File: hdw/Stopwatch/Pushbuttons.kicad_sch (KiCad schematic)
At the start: 41 parts, among them SW701 Cap_Touch, SW702 Cap_Touch, SW703 Cap_Touch, U701 AT42QT1010-TSHR, U702 TLV71330PDBV, U703 TLV71330PDBV, U704 74LVC1G80, U705 74LVC1G17, U706 TLV71330PDBV, U707 AT42QT1010-TSHR, U708 AT42QT1010-TSHR, U709 74LVC1G17, U710 74LVC1G17

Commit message: started sch work
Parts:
- removed C704, C707, C708, C709, C715: 0.1uF, Capacitors_SMD:C_0603, symbol Custom_Library:C_Custom
- removed C706: 10nF, Capacitors_SMD:C_0603, symbol Custom_Library:C_Custom
- removed C711: 10uF, Capacitors_SMD:C_0603, symbol Custom_Library:C_Custom
- removed R703: 499, Resistors_SMD:R_0603, symbol Custom_Library:R_Custom
- removed R710, R?: 10k, Resistors_SMD:R_0603, symbol Custom_Library:R_Custom
- removed SW703: Cap_Touch, Custom Footprints Library:Capacitive_Touch_Pad, symbol Custom_Library:Cap_Touch
- removed U702, U703, U706: TLV71330PDBV, Package_TO_SOT_SMD:SOT-23-5, symbol Incrementor-rescue:TLV71330PDBV-Regulator_Linear
- removed U705, U709, U710: 74LVC1G17, TO_SOT_Packages_SMD:SOT-353_SC-70-5, symbol Custom_Library:74LVC1G17_Power
- removed U708: AT42QT1010-TSHR, TO_SOT_Packages_SMD:SOT-23-6, symbol Sensor_Touch:AT42QT1010-TSHR
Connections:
- net +3V3: now also U701.5 (VDD), U701.6 (SYNC), U707.5 (VDD), U707.6 (SYNC)
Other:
- moved on the sheet: C701, C702, C703, C705, C712, C713, C717, R701, R702, R708, R709, R712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

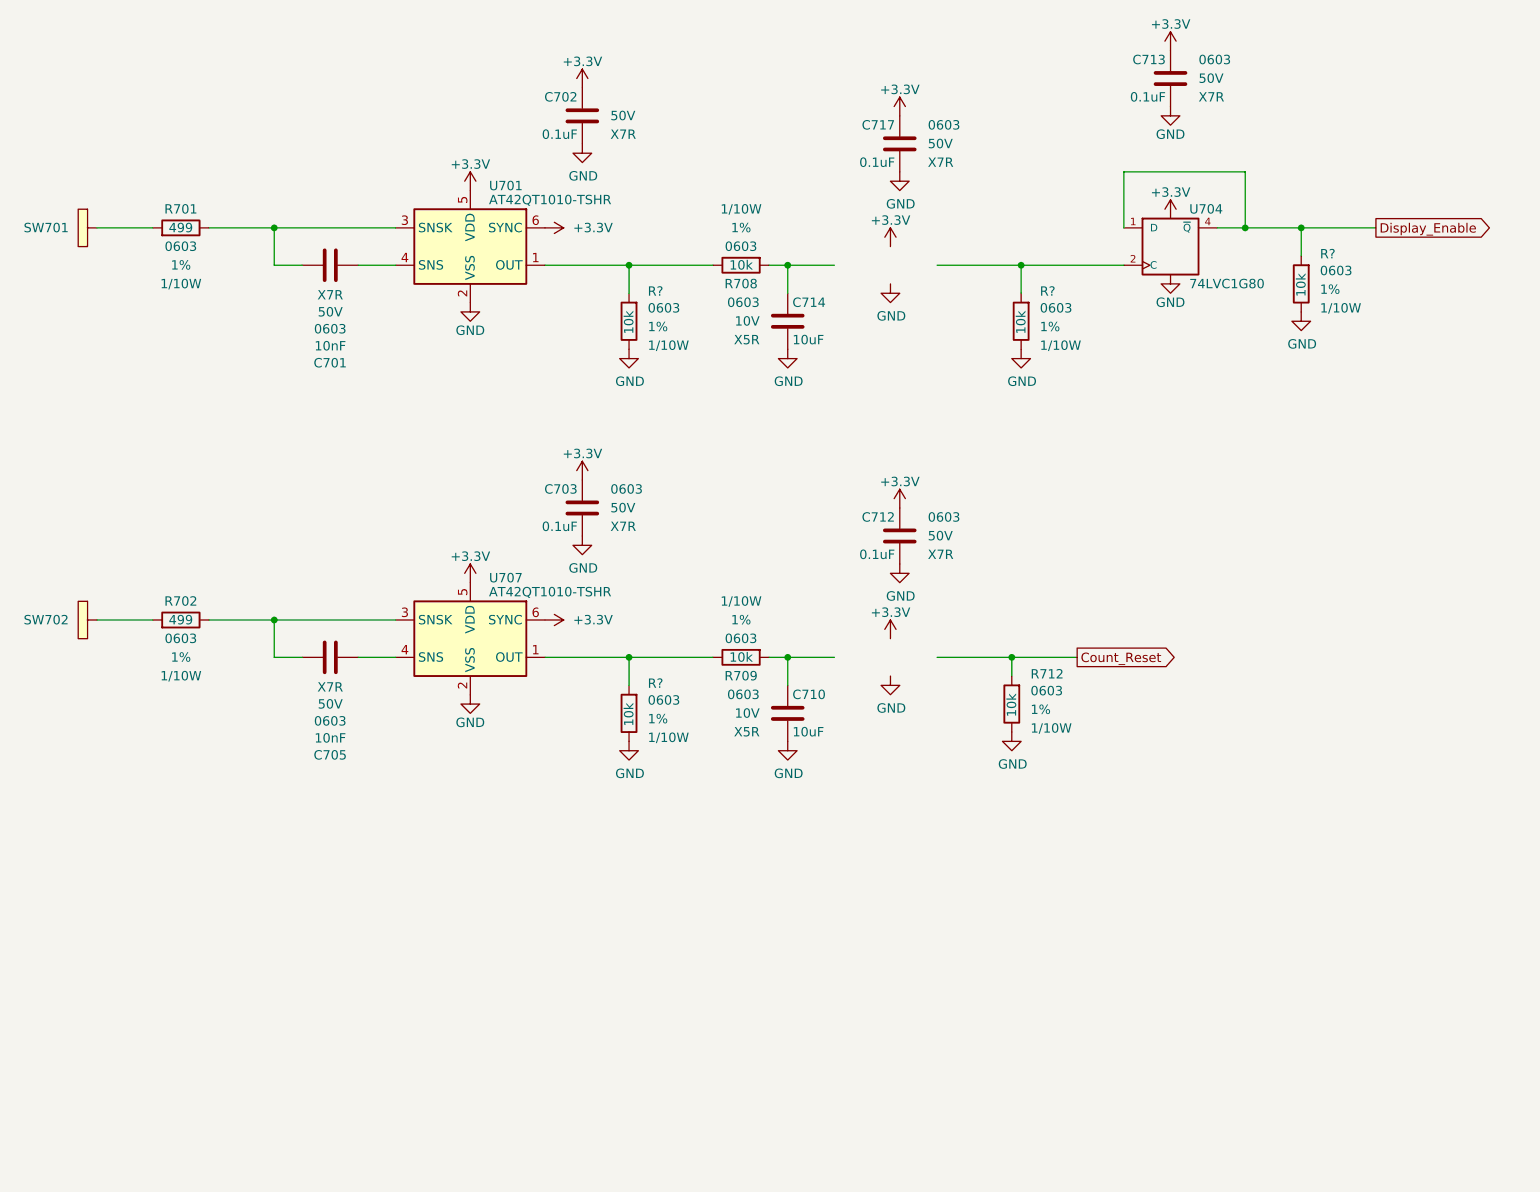
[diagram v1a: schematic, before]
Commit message: adjusted stage sheet
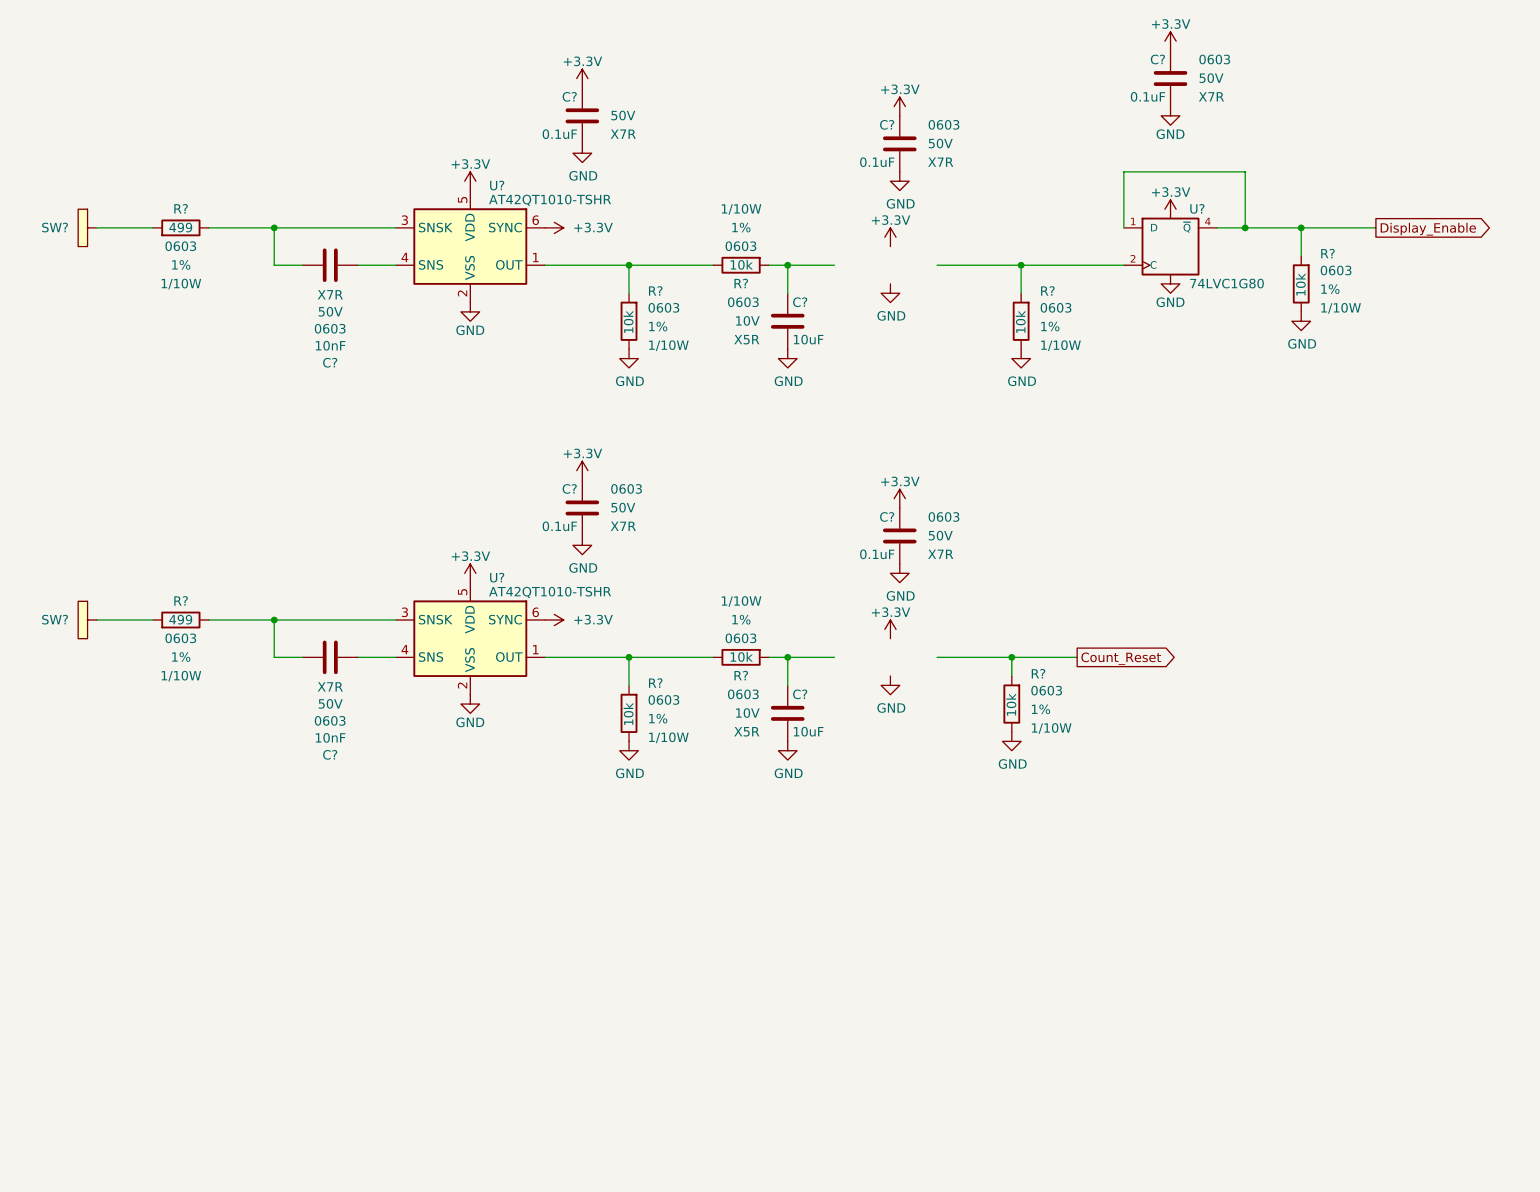
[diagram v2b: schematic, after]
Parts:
- renumbered C701 to C?, C713 to C?, C714 to C?, C702 to C?, C717 to C?, C705 to C?, C710 to C?, C712 to C?, C703 to C?, R701 to R?, R708 to R?, R712 to R?, R702 to R?, R709 to R?, SW701 to SW?, SW702 to SW?, U701 to U?, U704 to U?, U707 to U?

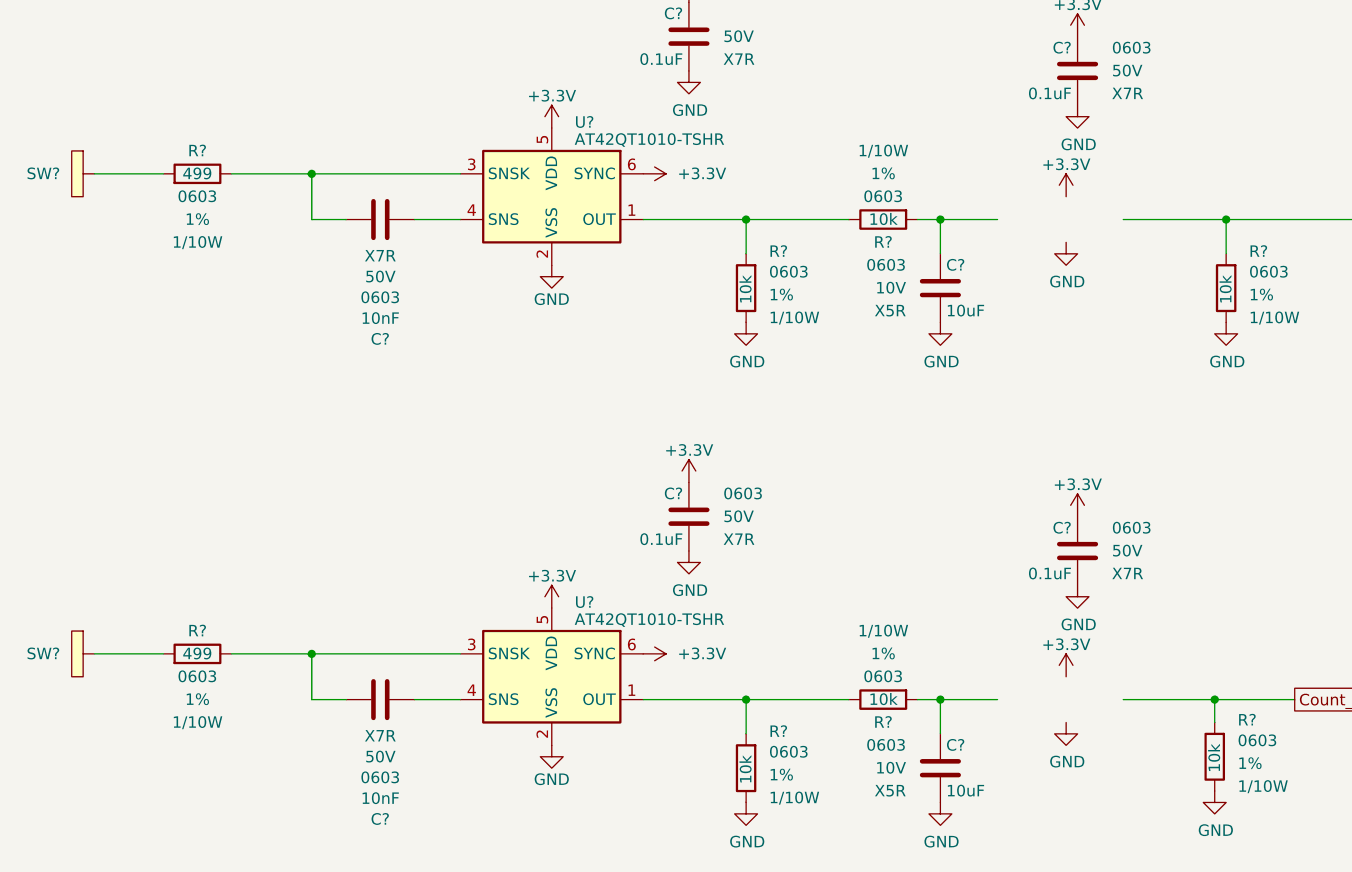
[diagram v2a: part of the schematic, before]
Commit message: added reset stuff
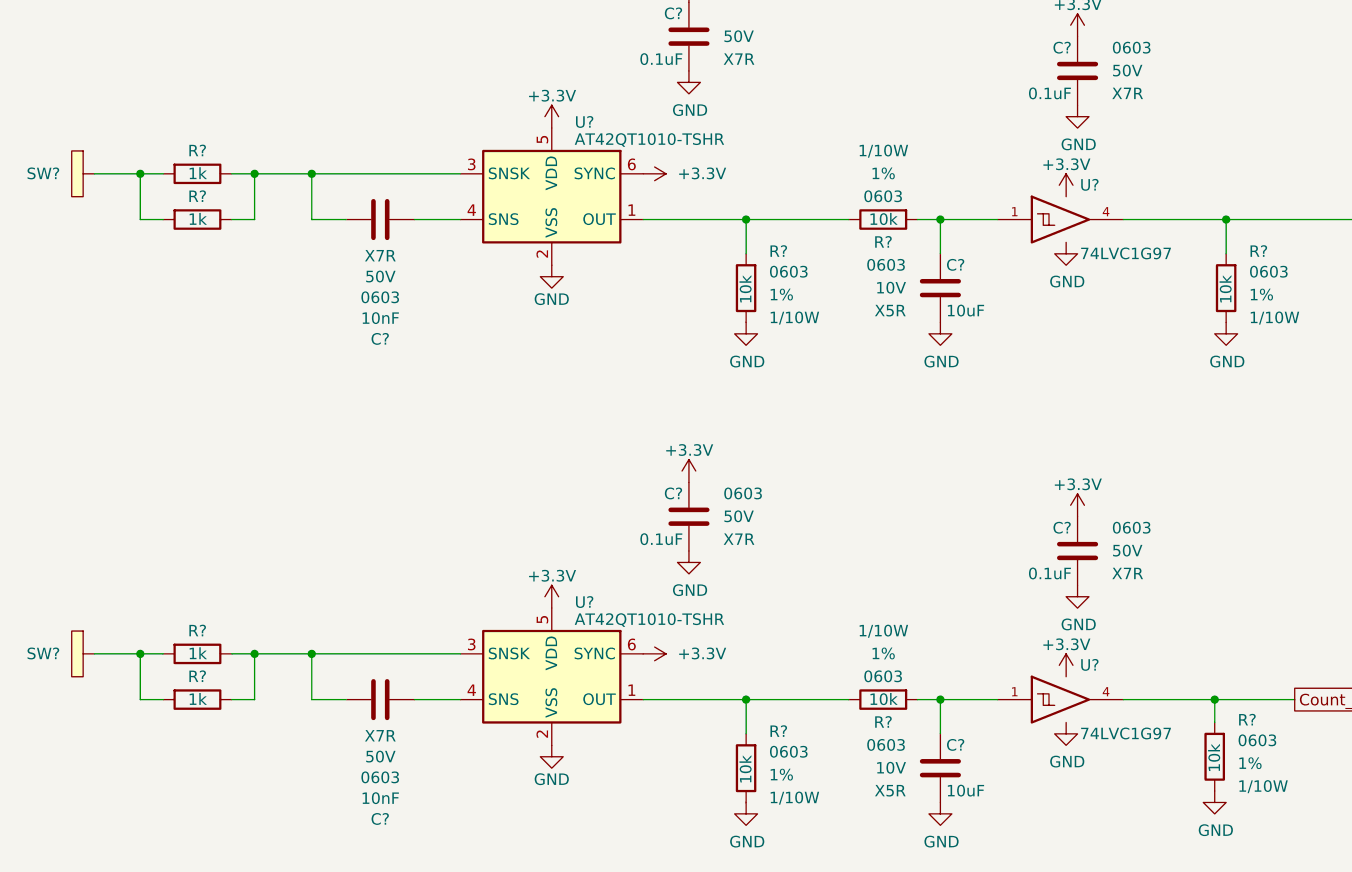
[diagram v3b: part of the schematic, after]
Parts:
- removed R? (x2): 499, Resistors_SMD:R_0603, symbol Custom_Library:R_Custom
- added R? (x4): 1k, Resistors_SMD:R_0603, symbol Custom_Library:R_Custom
- added U? (x2): 74LVC1G97, Package_TO_SOT_SMD:SOT-363_SC-70-6, symbol Custom Library:74LVC1G97_Power_BUF
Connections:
- net +3V3: now also U?.5 (VCC), U?.5 (VCC)
- net Count_Reset: now also U?.4
- net GND: now also U?.2 (GND), U?.2 (GND), U?.3 (GND), U?.3 (GND), U?.6 (GND), U?.6 (GND)
- net at C?.2, U?.3 (SNSK): now also R?.2, R?.2 (x2)
- net at SW?.1 (TP): now also R?.1, R?.1 (x2)
- net at R?.1, U?.2 (C): now also U?.4
- net at C?.1, R?.1: now also U?.1 (x2)

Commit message: added some more junk
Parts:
- added C?: 10nF, Capacitors_SMD:C_0603, symbol Custom_Library:C_Custom
- added C? (x3): 0.1uF, Capacitors_SMD:C_0603, symbol Custom_Library:C_Custom
- added C?: 10uF, Capacitors_SMD:C_0603, symbol Custom_Library:C_Custom
- added R? (x2): 1k, Resistors_SMD:R_0603, symbol Custom_Library:R_Custom
- added R? (x4): 10k, Resistors_SMD:R_0603, symbol Custom_Library:R_Custom
- added SW?: Cap_Touch, Custom Footprints Library:Capacitive_Touch_Pad, symbol Custom_Library:Cap_Touch
- added U?: 74LVC1G80, TO_SOT_Packages_SMD:SOT-353_SC-70-5, symbol Custom_Library:74LVC1G80_Power
- added U?: 74LVC1G97, Package_TO_SOT_SMD:SOT-363_SC-70-6, symbol Custom Library:74LVC1G97_Power_BUF
- added U?: AT42QT1010-TSHR, TO_SOT_Packages_SMD:SOT-23-6, symbol Sensor_Touch:AT42QT1010-TSHR
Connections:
- net +3V3: now also C?.1, C?.1, C?.1, U?.5 (VCC), U?.5 (VCC), U?.5 (VDD), U?.6 (SYNC)
- net GND: now also C?.2, C?.2, C?.2, C?.2, R?.2, R?.2, R?.2, U?.2 (GND), U?.2 (VSS), U?.3 (GND), U?.3 (GND), U?.6 (GND)
- new net: R?.1, R?.1, SW?.1 (TP)
- new net: C?.2, R?.2, R?.2, U?.3 (SNSK)
- new net: C?.1, R?.1, U?.1
- new net: R?.1, R?.2, U?.1 (OUT)
- new net: R?.1, U?.2 (C), U?.4
- new net: C?.1, U?.4 (SNS)
- new net Count_Enable: R?.1, U?.1 (D), U?.4 (~{Q})

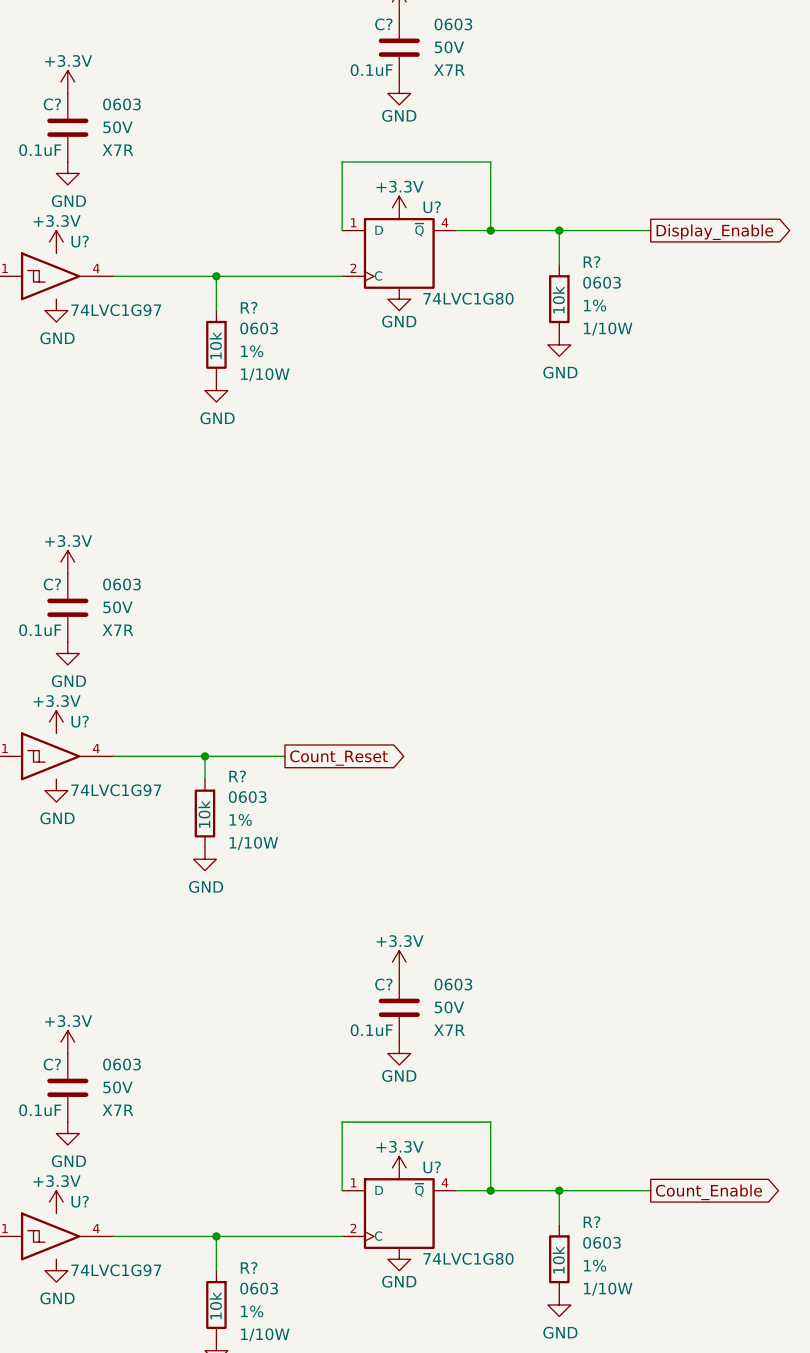
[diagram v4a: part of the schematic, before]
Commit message: reordered schematic sheets
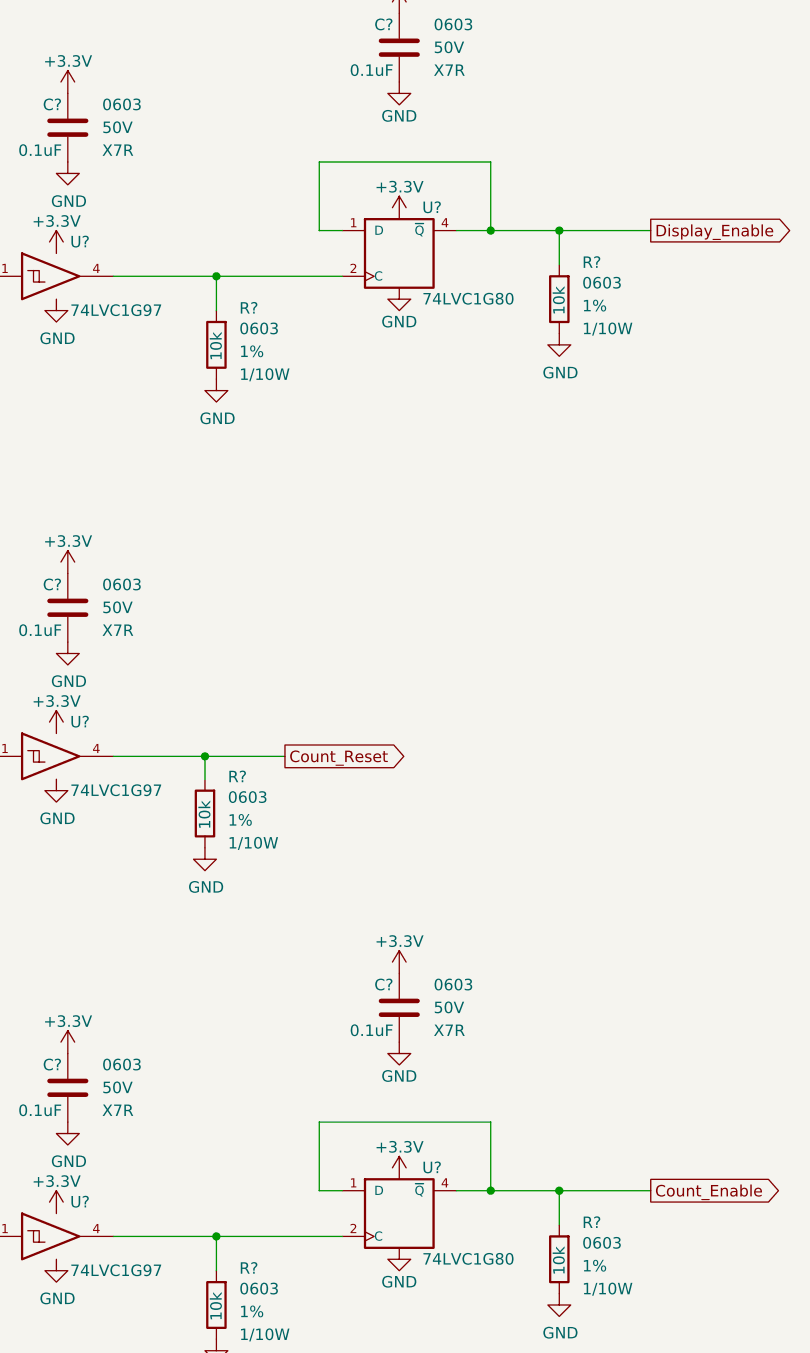
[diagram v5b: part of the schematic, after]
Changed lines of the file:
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@@
   (junction (at 142.24 100.33) (diameter 0) (color 0 0 0 0)
   )
+  (wire (pts (xy 185.42 148.59) (xy 187.96 148.59))
+    (stroke (width 0) (type default))
+  )
   (wire (pts (xy 63.5 148.59) (xy 66.04 148.59))
     (stroke (width 0) (type default))
@@
     (stroke (width 0) (type default))
   )
-  (wire (pts (xy 204.47 140.97) (xy 187.96 140.97))
+  (wire (pts (xy 204.47 140.97) (xy 185.42 140.97))
     (stroke (width 0) (type default))
   )
@@
     (stroke (width 0) (type default))
   )
+  (wire (pts (xy 185.42 41.91) (xy 187.96 41.91))
+    (stroke (width 0) (type default))
+  )
   (wire (pts (xy 187.96 46.99) (xy 173.99 46.99))
     (stroke (width 0) (type default))
@@
     (stroke (width 0) (type default))
   )
-  (wire (pts (xy 187.96 140.97) (xy 187.96 148.59))
+  (wire (pts (xy 185.42 140.97) (xy 185.42 148.59))
     (stroke (width 0) (type default))
   )
@@
     (stroke (width 0) (type default))
   )
-  (wire (pts (xy 187.96 34.29) (xy 187.96 41.91))
+  (wire (pts (xy 185.42 34.29) (xy 185.42 41.91))
     (stroke (width 0) (type default))
   )
@@
     (stroke (width 0) (type default))
   )
-  (wire (pts (xy 204.47 34.29) (xy 187.96 34.29))
-    (stroke (width 0) (type default))
-  )
+  (wire (pts (xy 204.47 34.29) (xy 185.42 34.29))
+    (stroke (width 0) (type default))
+  )
